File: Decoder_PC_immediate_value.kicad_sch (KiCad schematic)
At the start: 10 parts

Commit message: Finished Decoder Design
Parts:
- removed R4: 330Ω, Resistor_SMD:R_0805_2012Metric_Pad1.20x1.40mm_HandSolder, symbol Device:R
- removed TP4: AUX1, TestPoint:TestPoint_Pad_D1.0mm, symbol Connector:TestPoint
- added ControlByte1, Input1, Input2: ~, Other:8 Bit Bus Small, symbol Other:8_bit_mini_bus_bi
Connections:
- net AUX_1 is gone; now on net /CLK: U1.12 (A0)
- net ControlWord0: now also ControlByte1.1
- net ControlWord1: now also ControlByte1.2
- net ControlWord2: now also ControlByte1.3
- net ControlWord3: now also ControlByte1.4
- net ControlWord4: now also ControlByte1.5
- net ControlWord5: now also ControlByte1.6
- net ControlWord6: now also ControlByte1.7
- net ControlWord7: now also ControlByte1.8
- net OP_Code_1: now also Input1.1
- net OP_Code_2: now also Input1.2
- net OP_Code_3: now also Input1.3
- net OP_Code_4: now also Input1.4
- net OP_Code_5: now also Input1.5
- net OP_Code_6: now also Input1.6
- net OP_Code_7: now also Input1.7
- net OP_Code_8: now also Input1.8
- net OP_Code_9: now also Input2.8
- net PM: now also Input2.1
- net Stage_1: now also Input2.7
- net Stage_2: now also Input2.6
- net Stage_3: now also Input2.5
- net Stage_4: now also Input2.4
- net Stage_5: now also Input2.3
- net ZF: now also Input2.2

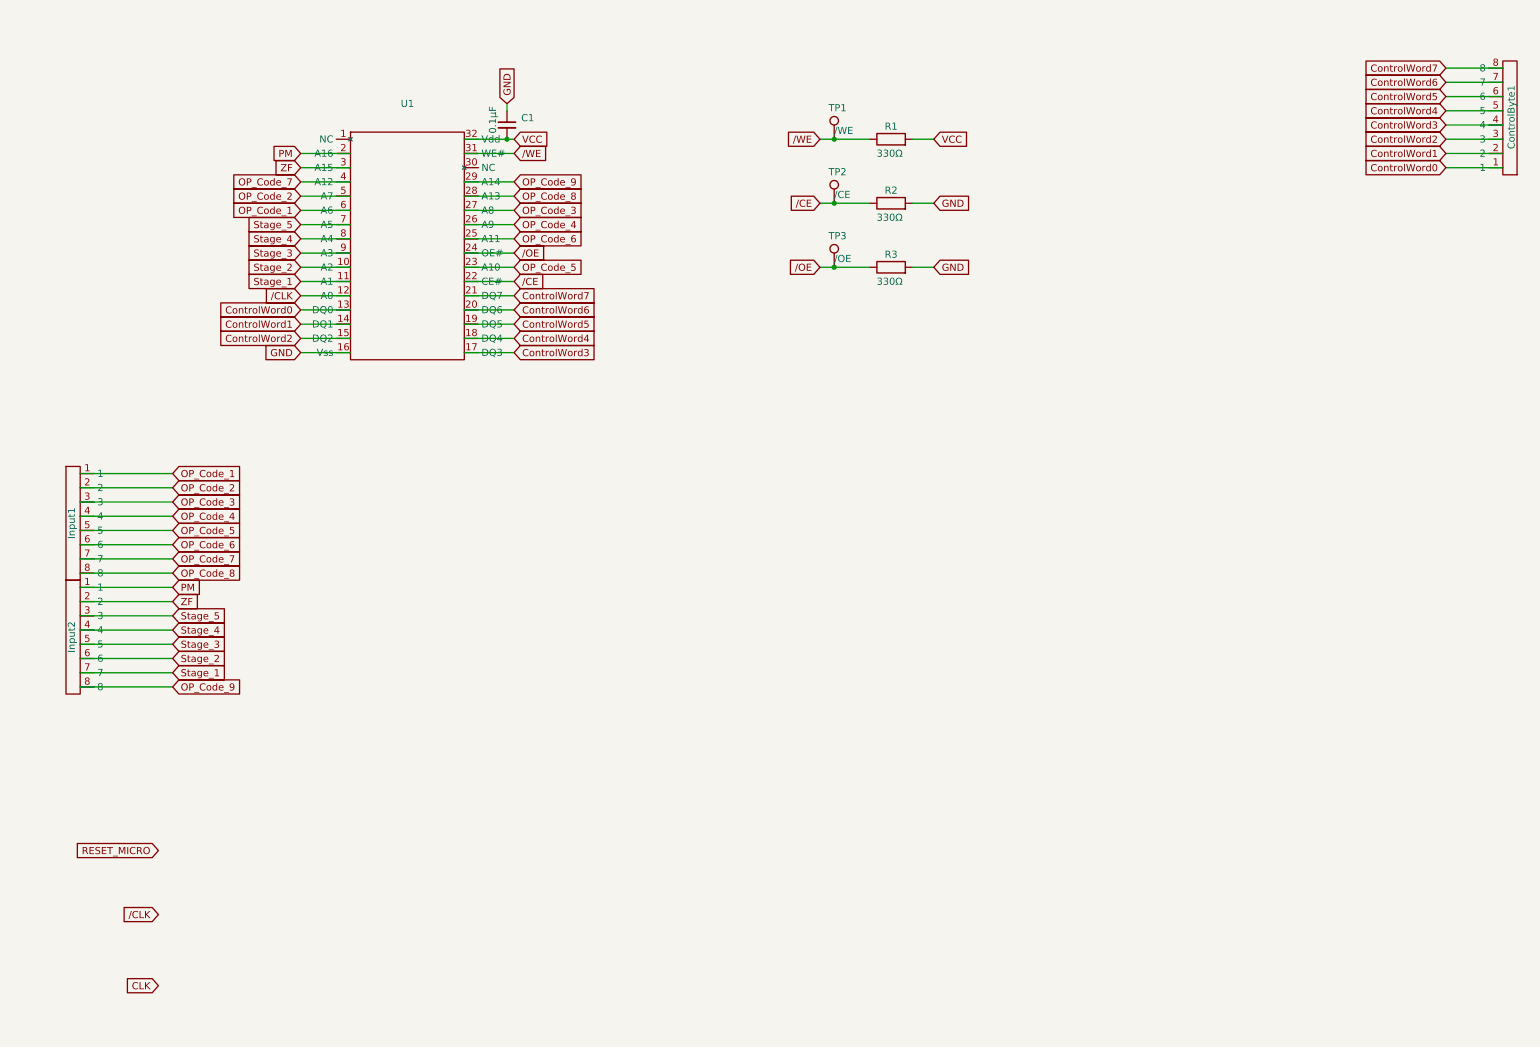
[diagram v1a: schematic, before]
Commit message: Added Decoder 1/2
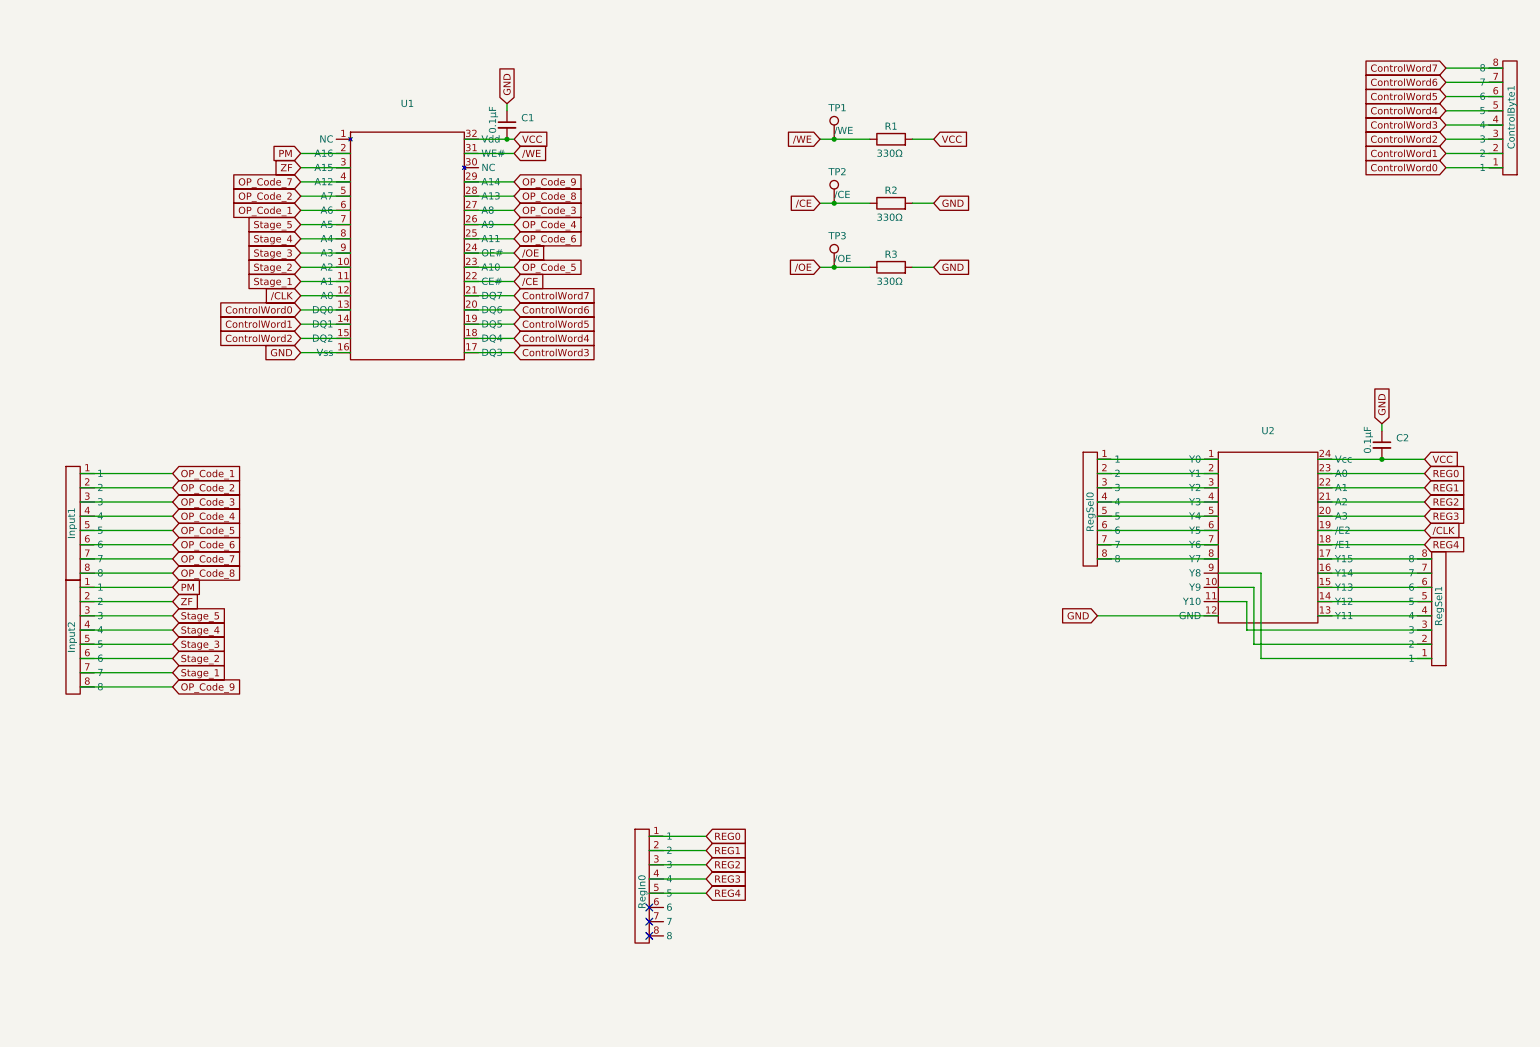
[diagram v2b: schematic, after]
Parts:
- added C2: 0.1µF, Capacitor_SMD:C_0805_2012Metric_Pad1.18x1.45mm_HandSolder, symbol Device:C_Small
- added RegIn0, RegSel0, RegSel1: ~, Other:8 Bit Bus Small, symbol Other:8_bit_mini_bus_bi
- added U2: ~, Package_SO:SOIC-24W_7.5x15.4mm_P1.27mm, symbol Texas Instrument Logic:CD54HC154
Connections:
- net GND: now also C2.1, U2.12 (GND)
- net VCC: now also C2.2, U2.24 (Vcc)
- net /CLK: now also U2.19 (/E2)
- new net: RegSel1.1, U2.9 (Y8)
- new net: RegSel1.2, U2.10 (Y9)
- new net: RegSel1.3, U2.11 (Y10)
- new net: RegSel1.4, U2.13 (Y11)
- new net: RegSel1.5, U2.14 (Y12)
- new net: RegSel1.6, U2.15 (Y13)
- new net: RegSel1.7, U2.16 (Y14)
- new net: RegSel1.8, U2.17 (Y15)
- new net: RegSel0.1, U2.1 (Y0)
- new net: RegSel0.2, U2.2 (Y1)
- new net: RegSel0.3, U2.3 (Y2)
- new net: RegSel0.4, U2.4 (Y3)
- new net: RegSel0.5, U2.5 (Y4)
- new net: RegSel0.6, U2.6 (Y5)
- new net: RegSel0.7, U2.7 (Y6)
- new net: RegSel0.8, U2.8 (Y7)
- new net REG0: RegIn0.1, U2.23 (A0)
- new net REG1: RegIn0.2, U2.22 (A1)
- new net REG2: RegIn0.3, U2.21 (A2)
- new net REG3: RegIn0.4, U2.20 (A3)
- new net REG4: RegIn0.5, U2.18 (/E1)
- no-connect marks 0 -> 3

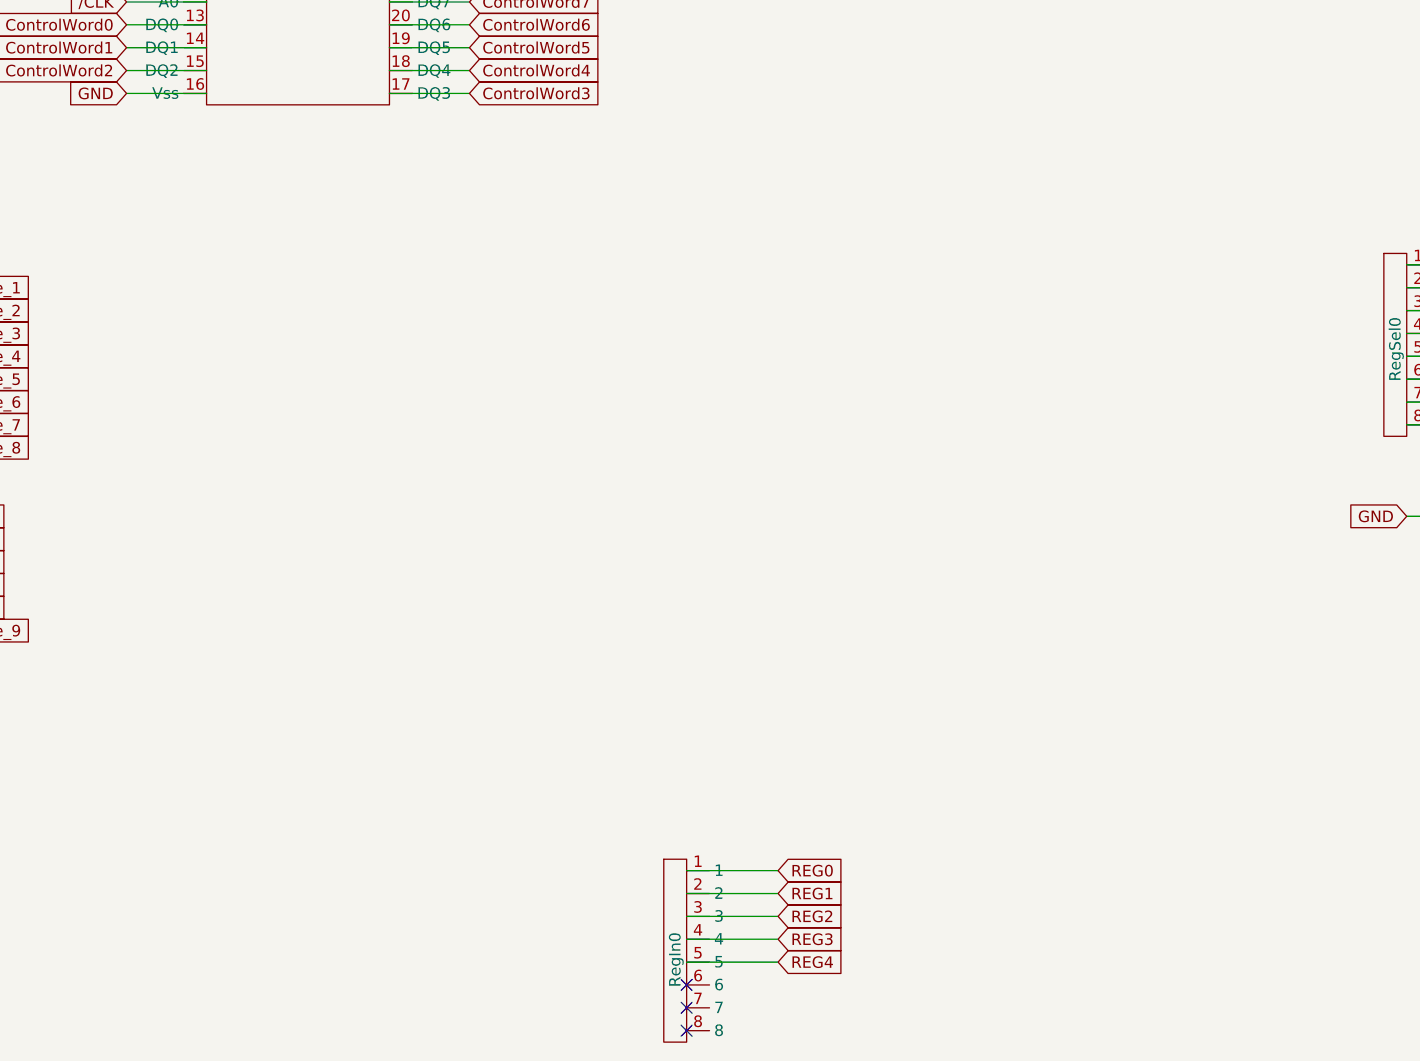
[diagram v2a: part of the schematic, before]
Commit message: Schematic for Second Decoder
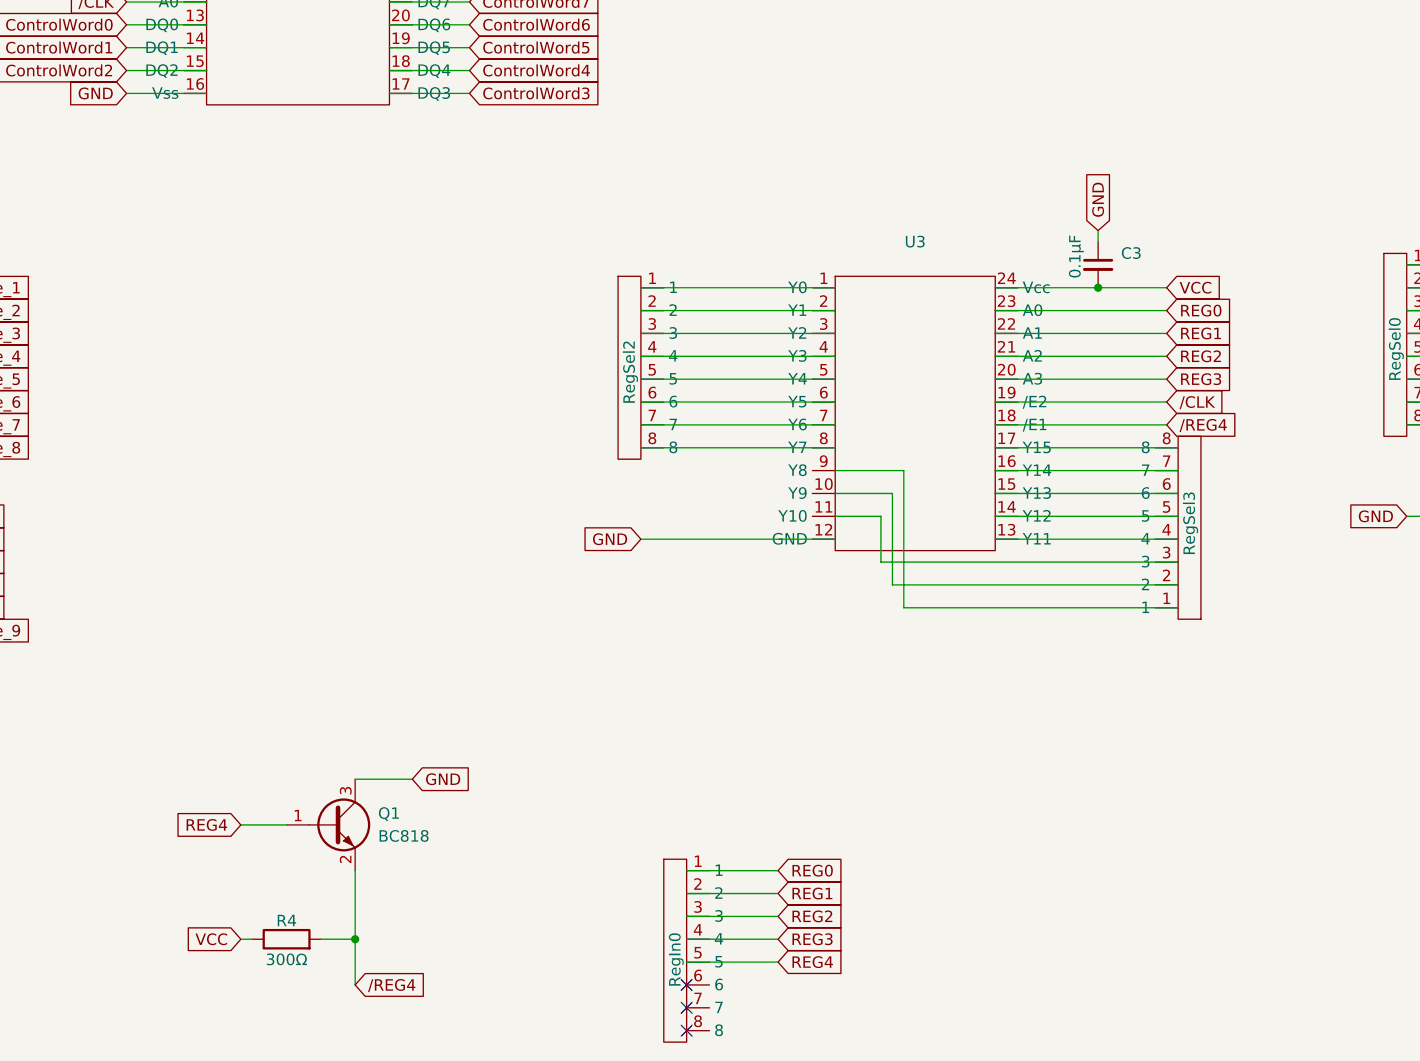
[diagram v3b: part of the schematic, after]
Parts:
- added C3: 0.1µF, Capacitor_SMD:C_0805_2012Metric_Pad1.18x1.45mm_HandSolder, symbol Device:C_Small
- added Q1: BC818, Package_TO_SOT_SMD:SOT-23, symbol Transistor_BJT:BC818
- added R4: 300Ω, Resistor_SMD:R_0805_2012Metric_Pad1.20x1.40mm_HandSolder, symbol Device:R
- added RegSel2, RegSel3: ~, Other:8 Bit Bus Small, symbol Other:8_bit_mini_bus_bi
- added U3: ~, Package_SO:SOIC-24W_7.5x15.4mm_P1.27mm, symbol Texas Instrument Logic:CD54HC154
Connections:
- net GND: now also C3.1, Q1.3 (C), U3.12 (GND)
- net REG0: now also U3.23 (A0)
- net REG1: now also U3.22 (A1)
- net REG2: now also U3.21 (A2)
- net REG3: now also U3.20 (A3)
- net REG4: now also Q1.1 (B)
- net VCC: now also C3.2, R4.1, U3.24 (Vcc)
- net /CLK: now also U3.19 (/E2)
- new net: RegSel2.1, U3.1 (Y0)
- new net: RegSel3.2, U3.10 (Y9)
- new net: RegSel3.3, U3.11 (Y10)
- new net: RegSel3.4, U3.13 (Y11)
- new net: RegSel3.5, U3.14 (Y12)
- new net: RegSel3.6, U3.15 (Y13)
- new net: RegSel3.7, U3.16 (Y14)
- new net: RegSel3.8, U3.17 (Y15)
- new net: RegSel2.2, U3.2 (Y1)
- new net: RegSel2.3, U3.3 (Y2)
- new net: RegSel2.4, U3.4 (Y3)
- new net: RegSel2.5, U3.5 (Y4)
- new net: RegSel2.6, U3.6 (Y5)
- new net: RegSel2.7, U3.7 (Y6)
- new net: RegSel2.8, U3.8 (Y7)
- new net: RegSel3.1, U3.9 (Y8)
- new net /REG4: Q1.2 (E), R4.2, U3.18 (/E1)

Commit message: Added Power Source
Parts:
- added B1: ~, Other:Single Bit Bus, symbol Other:Single_Bit_Bus
- added D1: D, Diode_THT:D_5W_P10.16mm_Horizontal, symbol Device:D
- added U5: ~, Other:Vcc & GND, symbol Other:Vcc_&_GND
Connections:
- net GND: now also U5.2 (GND)
- net VCC: now also D1.1 (K)
- net /CLK: now also B1.1
- new net: D1.2 (A), U5.1 (Vcc)

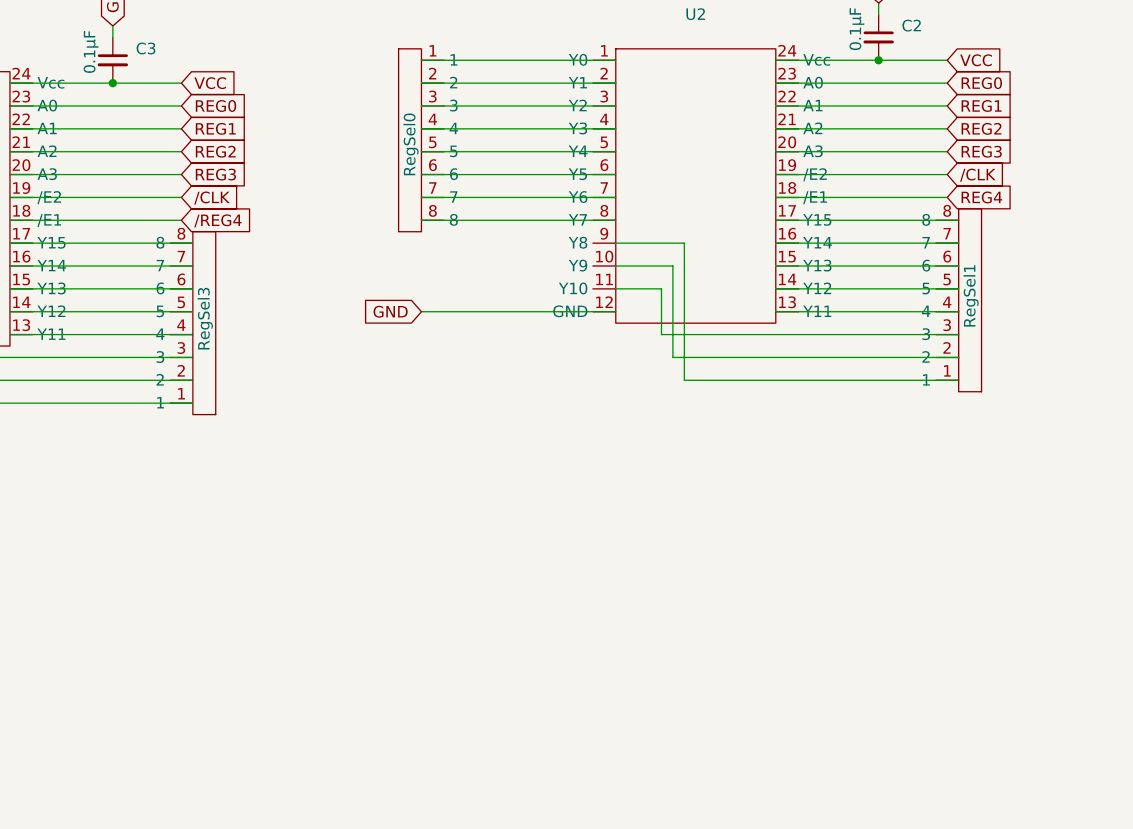
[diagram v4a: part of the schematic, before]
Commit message: Corrected Addressing Of Decoders
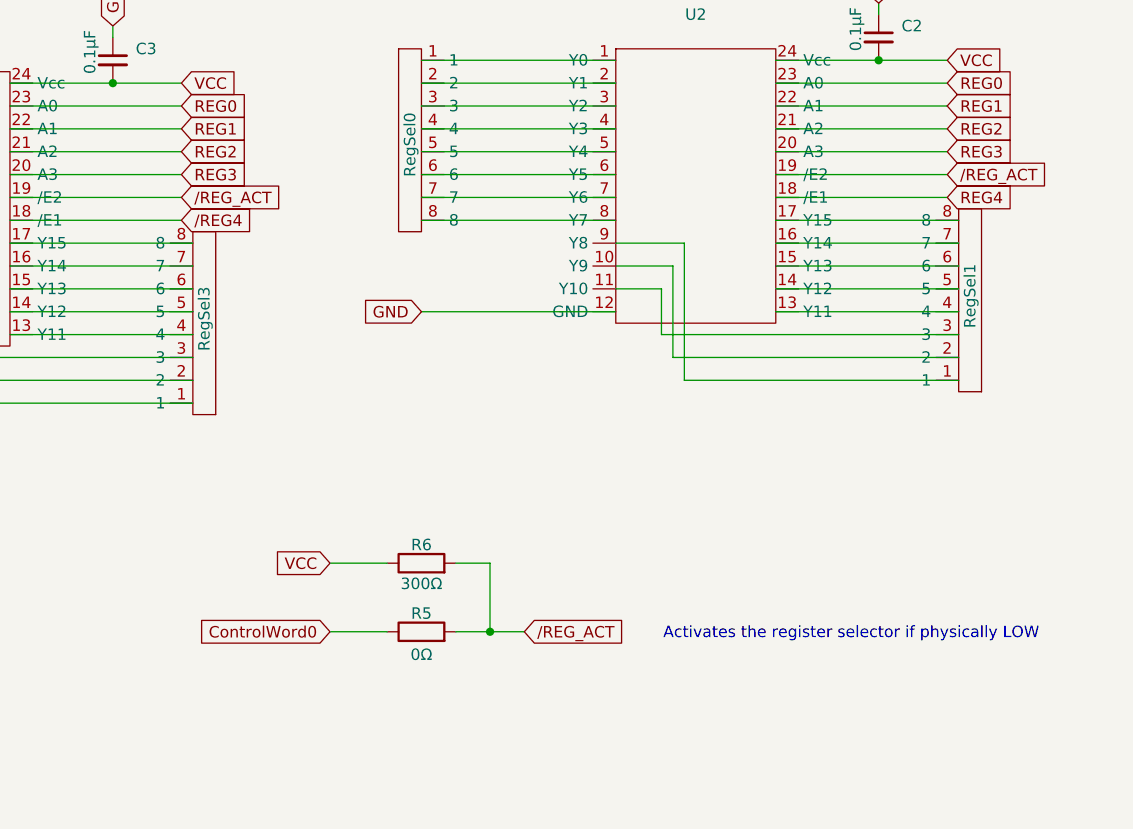
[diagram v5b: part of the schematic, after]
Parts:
- added R5: 0Ω, Resistor_SMD:R_0805_2012Metric_Pad1.20x1.40mm_HandSolder, symbol Device:R
- added R6: 300Ω, Resistor_SMD:R_0805_2012Metric_Pad1.20x1.40mm_HandSolder, symbol Device:R
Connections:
- net ControlWord0: now also R5.1
- net VCC: now also R6.1
- net /CLK: no longer U2.19 (/E2), U3.19 (/E2)
- new net /REG_ACT: R5.2, R6.2, U2.19 (/E2), U3.19 (/E2)
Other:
- note added: "Activates the register selector if physically LOW"
